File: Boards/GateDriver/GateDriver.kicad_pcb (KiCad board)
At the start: 6 copper layers, 75 x 60 mm, 69 parts, among them IC1 ADUM4136BRWZ, IC2 ADUM4136BRWZ, J1 Conn_02x08_Counter_Clockwise

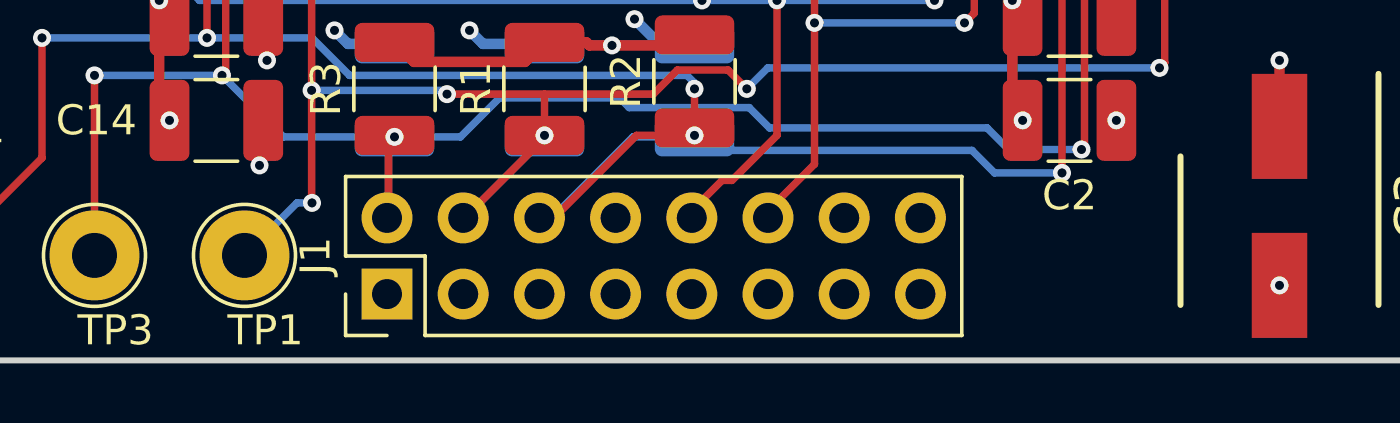
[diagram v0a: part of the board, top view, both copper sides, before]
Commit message: fix connector pinout
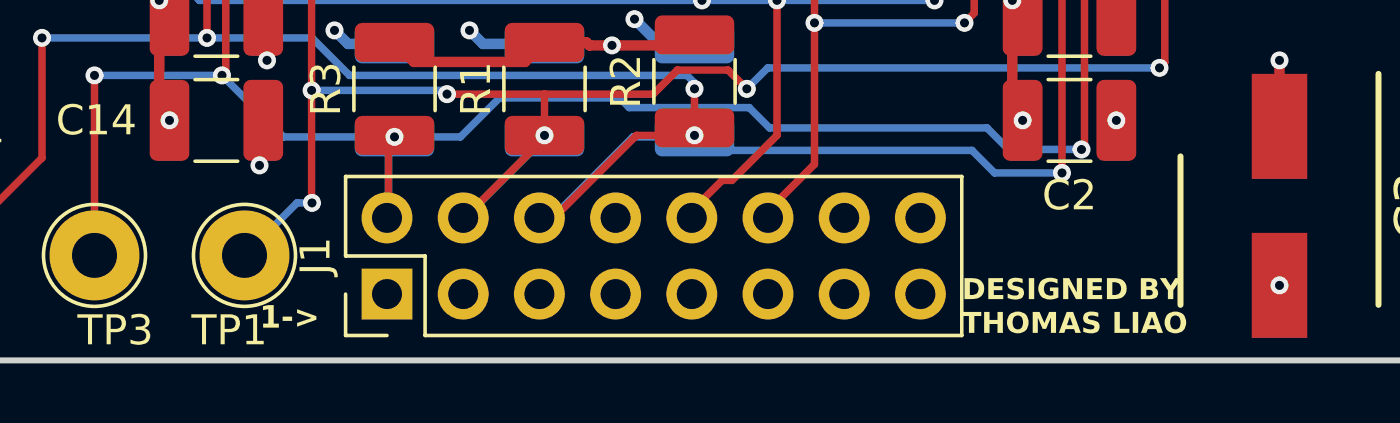
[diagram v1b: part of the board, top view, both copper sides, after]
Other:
- board text added: "1->"
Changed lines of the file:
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@@
 		(tags "test point wire loop bead")
 		(property "Reference" "TP1"
-			(at 0.7 2.5 0)
+			(at -0.5 2.5 0)
 			(layer "F.SilkS")
 			(effects
@@
 		)
 	)
+	(gr_text "1->"
+		(at 25.5 59 0)
+		(layer "F.SilkS")
+		(effects
+			(font
+				(size 0.75 0.75)
+				(thickness 0.1875)
+				(bold yes)
+			)
+			(justify left bottom)
+		)
+	)
 	(gr_text "DANGER HIGH VOLTAGE"
 		(at 58.5 39 0)
@@
 		)
 	)
+	(gr_text "DESIGNED BY\nTHOMAS LIAO"
+		(at 48.91 59.17 0)
+		(layer "F.SilkS")
+		(effects
+			(font
+				(size 0.7 0.7)
+				(thickness 0.175)
+				(bold yes)
+			)
+			(justify left bottom)
+		)
+	)
 	(gr_text "62MM POWER MODULE DRIVER\nREV 1\n1200VMAX, 800V WORKING"
 		(at 0 39.5 0)
@@
 		)
 	)
-	(gr_text "DESIGNED BY\nTHOMAS LIAO"
-		(at 58.5 59 -0)
-		(layer "B.SilkS")
-		(effects
-			(font
-				(size 0.7 0.7)
-				(thickness 0.175)
-				(bold yes)
-			)
-			(justify left bottom mirror)
-		)
-	)
